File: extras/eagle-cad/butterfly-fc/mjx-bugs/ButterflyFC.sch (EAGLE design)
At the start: 5 parts

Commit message: Added sodler pads
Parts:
- added PAD1, PAD10, PAD2, PAD3, PAD4, PAD5, PAD6, PAD7, PAD8, PAD9: (no value), wirepad:SMD5
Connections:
- net GND: now also PAD10.P, PAD2.P, PAD4.P, PAD6.P, PAD8.P
- net VBAT: now also PAD1.P, PAD3.P, PAD5.P, PAD7.P, PAD9.P
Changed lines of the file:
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@@
 <part name="5VREG" library="SparkFun-Connectors" deviceset="CONN_03" device="1X03_NO_SILK"/>
 <part name="USFS" library="SparkFun-Connectors" deviceset="CONN_05" device="NO_SILK"/>
+<part name="PAD1" library="wirepad" deviceset="SMD5" device=""/>
+<part name="PAD2" library="wirepad" deviceset="SMD5" device=""/>
+<part name="PAD3" library="wirepad" deviceset="SMD5" device=""/>
+<part name="PAD4" library="wirepad" deviceset="SMD5" device=""/>
+<part name="PAD5" library="wirepad" deviceset="SMD5" device=""/>
+<part name="PAD6" library="wirepad" deviceset="SMD5" device=""/>
+<part name="PAD7" library="wirepad" deviceset="SMD5" device=""/>
+<part name="PAD8" library="wirepad" deviceset="SMD5" device=""/>
+<part name="PAD9" library="wirepad" deviceset="SMD5" device=""/>
+<part name="PAD10" library="wirepad" deviceset="SMD5" device=""/>
 </parts>
 <sheets>
@@
 <attribute name="NAME" x="38.1" y="56.388" size="1.778" layer="95" font="vector"/>
 </instance>
+<instance part="PAD1" gate="1" x="15.24" y="139.7" smashed="yes">
+<attribute name="VALUE" x="14.097" y="136.398" size="1.778" layer="96"/>
+</instance>
+<instance part="PAD2" gate="1" x="15.24" y="129.54" smashed="yes">
+<attribute name="VALUE" x="14.097" y="126.238" size="1.778" layer="96"/>
+</instance>
+<instance part="PAD3" gate="1" x="35.56" y="139.7" smashed="yes">
+<attribute name="VALUE" x="34.417" y="136.398" size="1.778" layer="96"/>
+</instance>
+<instance part="PAD4" gate="1" x="35.56" y="129.54" smashed="yes">
+<attribute name="VALUE" x="34.417" y="126.238" size="1.778" layer="96"/>
+</instance>
+<instance part="PAD5" gate="1" x="53.34" y="139.7" smashed="yes">
+<attribute name="VALUE" x="52.197" y="136.398" size="1.778" layer="96"/>
+</instance>
+<instance part="PAD6" gate="1" x="53.34" y="129.54" smashed="yes">
+<attribute name="VALUE" x="52.197" y="126.238" size="1.778" layer="96"/>
+</instance>
+<instance part="PAD7" gate="1" x="73.66" y="139.7" smashed="yes">
+<attribute name="VALUE" x="72.517" y="136.398" size="1.778" layer="96"/>
+</instance>
+<instance part="PAD8" gate="1" x="73.66" y="129.54" smashed="yes">
+<attribute name="VALUE" x="72.517" y="126.238" size="1.778" layer="96"/>
+</instance>
+<instance part="PAD9" gate="1" x="91.44" y="139.7" smashed="yes">
+<attribute name="VALUE" x="90.297" y="136.398" size="1.778" layer="96"/>
+</instance>
+<instance part="PAD10" gate="1" x="91.44" y="129.54" smashed="yes">
+<attribute name="VALUE" x="90.297" y="126.238" size="1.778" layer="96"/>
+</instance>
 </instances>
 <busses>
@@
 <label x="48.26" y="53.34" size="1.778" layer="95"/>
 </segment>
+<segment>
+<pinref part="PAD2" gate="1" pin="P"/>
+<wire x1="17.78" y1="129.54" x2="22.86" y2="129.54" width="0.1524" layer="91"/>
+<label x="17.78" y="129.54" size="1.778" layer="95"/>
+</segment>
+<segment>
+<pinref part="PAD4" gate="1" pin="P"/>
+<wire x1="38.1" y1="129.54" x2="43.18" y2="129.54" width="0.1524" layer="91"/>
+<label x="38.1" y="129.54" size="1.778" layer="95"/>
+</segment>
+<segment>
+<pinref part="PAD6" gate="1" pin="P"/>
+<wire x1="55.88" y1="129.54" x2="60.96" y2="129.54" width="0.1524" layer="91"/>
+<label x="55.88" y="129.54" size="1.778" layer="95"/>
+</segment>
+<segment>
+<pinref part="PAD8" gate="1" pin="P"/>
+<wire x1="76.2" y1="129.54" x2="81.28" y2="129.54" width="0.1524" layer="91"/>
+<label x="76.2" y="129.54" size="1.778" layer="95"/>
+</segment>
+<segment>
+<pinref part="PAD10" gate="1" pin="P"/>
+<wire x1="93.98" y1="129.54" x2="99.06" y2="129.54" width="0.1524" layer="91"/>
+<label x="93.98" y="129.54" size="1.778" layer="95"/>
+</segment>
 </net>
 <net name="5V" class="0">
@@
 <label x="53.34" y="78.74" size="1.778" layer="95"/>
 </segment>
-</net>
+<segment>
+<pinref part="PAD1" gate="1" pin="P"/>
+<wire x1="17.78" y1="139.7" x2="22.86" y2="139.7" width="0.1524" layer="91"/>
+<label x="17.78" y="139.7" size="1.778" layer="95"/>
+</segment>
+<segment>
+<pinref part="PAD3" gate="1" pin="P"/>
+<wire x1="38.1" y1="139.7" x2="43.18" y2="139.7" width="0.1524" layer="91"/>
+<label x="38.1" y="139.7" size="1.778" layer="95"/>
+</segment>
+<segment>
+<pinref part="PAD5" gate="1" pin="P"/>
+<wire x1="55.88" y1="139.7" x2="60.96" y2="139.7" width="0.1524" layer="91"/>
+<label x="55.88" y="139.7" size="1.778" layer="95"/>
+</segment>
+<segment>
+<pinref part="PAD7" gate="1" pin="P"/>
+<wire x1="76.2" y1="139.7" x2="81.28" y2="139.7" width="0.1524" layer="91"/>
+<label x="76.2" y="139.7" size="1.778" layer="95"/>
+</segment>
+<segment>
+<pinref part="PAD9" gate="1" pin="P"/>
+<wire x1="93.98" y1="139.7" x2="99.06" y2="139.7" width="0.1524" layer="91"/>
+<label x="93.98" y="139.7" size="1.778" layer="95"/>
+</segment>
+</net>

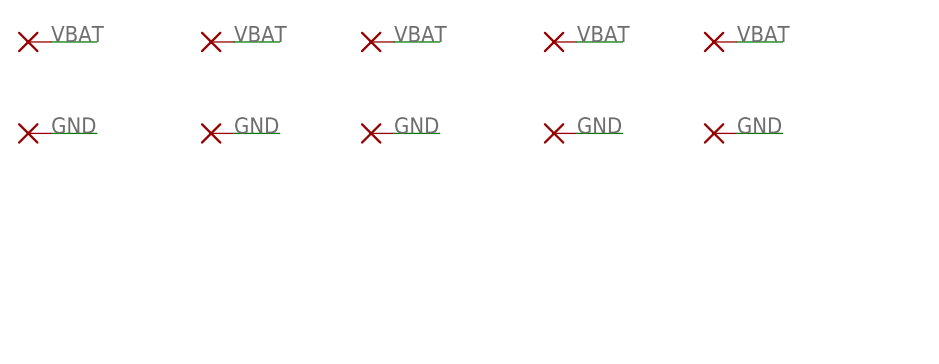
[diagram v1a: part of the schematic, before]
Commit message: Adjusted holes in board
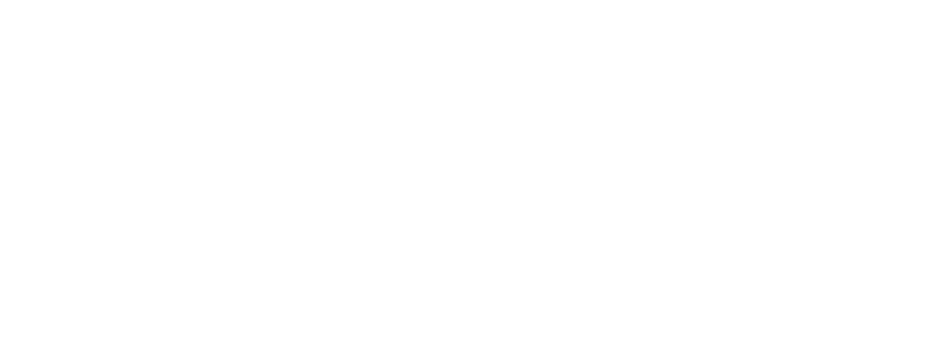
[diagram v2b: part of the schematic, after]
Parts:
- removed PAD1, PAD10, PAD2, PAD3, PAD4, PAD5, PAD6, PAD7, PAD8, PAD9: (no value), wirepad:SMD5
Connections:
- net GND: no longer PAD10.P, PAD2.P, PAD4.P, PAD6.P, PAD8.P
- net VBAT: no longer PAD1.P, PAD3.P, PAD5.P, PAD7.P, PAD9.P
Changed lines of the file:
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@@
 <part name="5VREG" library="SparkFun-Connectors" deviceset="CONN_03" device="1X03_NO_SILK"/>
 <part name="USFS" library="SparkFun-Connectors" deviceset="CONN_05" device="NO_SILK"/>
-<part name="PAD1" library="wirepad" deviceset="SMD5" device=""/>
-<part name="PAD2" library="wirepad" deviceset="SMD5" device=""/>
-<part name="PAD3" library="wirepad" deviceset="SMD5" device=""/>
-<part name="PAD4" library="wirepad" deviceset="SMD5" device=""/>
-<part name="PAD5" library="wirepad" deviceset="SMD5" device=""/>
-<part name="PAD6" library="wirepad" deviceset="SMD5" device=""/>
-<part name="PAD7" library="wirepad" deviceset="SMD5" device=""/>
-<part name="PAD8" library="wirepad" deviceset="SMD5" device=""/>
-<part name="PAD9" library="wirepad" deviceset="SMD5" device=""/>
-<part name="PAD10" library="wirepad" deviceset="SMD5" device=""/>
 </parts>
 <sheets>
@@
 <attribute name="VALUE" x="38.1" y="38.354" size="1.778" layer="96" font="vector"/>
 <attribute name="NAME" x="38.1" y="56.388" size="1.778" layer="95" font="vector"/>
-</instance>
-<instance part="PAD1" gate="1" x="15.24" y="139.7" smashed="yes">
-<attribute name="VALUE" x="14.097" y="136.398" size="1.778" layer="96"/>
-</instance>
-<instance part="PAD2" gate="1" x="15.24" y="129.54" smashed="yes">
-<attribute name="VALUE" x="14.097" y="126.238" size="1.778" layer="96"/>
-</instance>
-<instance part="PAD3" gate="1" x="35.56" y="139.7" smashed="yes">
-<attribute name="VALUE" x="34.417" y="136.398" size="1.778" layer="96"/>
-</instance>
-<instance part="PAD4" gate="1" x="35.56" y="129.54" smashed="yes">
-<attribute name="VALUE" x="34.417" y="126.238" size="1.778" layer="96"/>
-</instance>
-<instance part="PAD5" gate="1" x="53.34" y="139.7" smashed="yes">
-<attribute name="VALUE" x="52.197" y="136.398" size="1.778" layer="96"/>
-</instance>
-<instance part="PAD6" gate="1" x="53.34" y="129.54" smashed="yes">
-<attribute name="VALUE" x="52.197" y="126.238" size="1.778" layer="96"/>
-</instance>
-<instance part="PAD7" gate="1" x="73.66" y="139.7" smashed="yes">
-<attribute name="VALUE" x="72.517" y="136.398" size="1.778" layer="96"/>
-</instance>
-<instance part="PAD8" gate="1" x="73.66" y="129.54" smashed="yes">
-<attribute name="VALUE" x="72.517" y="126.238" size="1.778" layer="96"/>
-</instance>
-<instance part="PAD9" gate="1" x="91.44" y="139.7" smashed="yes">
-<attribute name="VALUE" x="90.297" y="136.398" size="1.778" layer="96"/>
-</instance>
-<instance part="PAD10" gate="1" x="91.44" y="129.54" smashed="yes">
-<attribute name="VALUE" x="90.297" y="126.238" size="1.778" layer="96"/>
 </instance>
 </instances>
@@
 <wire x1="48.26" y1="53.34" x2="53.34" y2="53.34" width="0.1524" layer="91"/>
 <label x="48.26" y="53.34" size="1.778" layer="95"/>
-</segment>
-<segment>
-<pinref part="PAD2" gate="1" pin="P"/>
-<wire x1="17.78" y1="129.54" x2="22.86" y2="129.54" width="0.1524" layer="91"/>
-<label x="17.78" y="129.54" size="1.778" layer="95"/>
-</segment>
-<segment>
-<pinref part="PAD4" gate="1" pin="P"/>
-<wire x1="38.1" y1="129.54" x2="43.18" y2="129.54" width="0.1524" layer="91"/>
-<label x="38.1" y="129.54" size="1.778" layer="95"/>
-</segment>
-<segment>
-<pinref part="PAD6" gate="1" pin="P"/>
-<wire x1="55.88" y1="129.54" x2="60.96" y2="129.54" width="0.1524" layer="91"/>
-<label x="55.88" y="129.54" size="1.778" layer="95"/>
-</segment>
-<segment>
-<pinref part="PAD8" gate="1" pin="P"/>
-<wire x1="76.2" y1="129.54" x2="81.28" y2="129.54" width="0.1524" layer="91"/>
-<label x="76.2" y="129.54" size="1.778" layer="95"/>
-</segment>
-<segment>
-<pinref part="PAD10" gate="1" pin="P"/>
-<wire x1="93.98" y1="129.54" x2="99.06" y2="129.54" width="0.1524" layer="91"/>
-<label x="93.98" y="129.54" size="1.778" layer="95"/>
 </segment>
 </net>
@@
 <label x="53.34" y="78.74" size="1.778" layer="95"/>
 </segment>
-<segment>
-<pinref part="PAD1" gate="1" pin="P"/>
-<wire x1="17.78" y1="139.7" x2="22.86" y2="139.7" width="0.1524" layer="91"/>
-<label x="17.78" y="139.7" size="1.778" layer="95"/>
-</segment>
-<segment>
-<pinref part="PAD3" gate="1" pin="P"/>
-<wire x1="38.1" y1="139.7" x2="43.18" y2="139.7" width="0.1524" layer="91"/>
-<label x="38.1" y="139.7" size="1.778" layer="95"/>
-</segment>
-<segment>
-<pinref part="PAD5" gate="1" pin="P"/>
-<wire x1="55.88" y1="139.7" x2="60.96" y2="139.7" width="0.1524" layer="91"/>
-<label x="55.88" y="139.7" size="1.778" layer="95"/>
-</segment>
-<segment>
-<pinref part="PAD7" gate="1" pin="P"/>
-<wire x1="76.2" y1="139.7" x2="81.28" y2="139.7" width="0.1524" layer="91"/>
-<label x="76.2" y="139.7" size="1.778" layer="95"/>
-</segment>
-<segment>
-<pinref part="PAD9" gate="1" pin="P"/>
-<wire x1="93.98" y1="139.7" x2="99.06" y2="139.7" width="0.1524" layer="91"/>
-<label x="93.98" y="139.7" size="1.778" layer="95"/>
-</segment>
 </net>

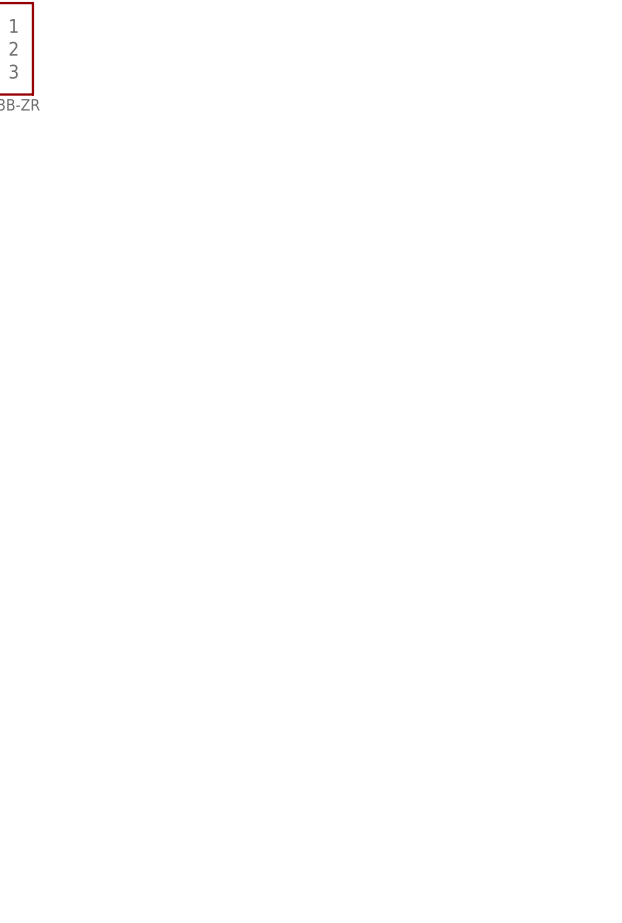
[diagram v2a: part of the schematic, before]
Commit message: Added solder pads
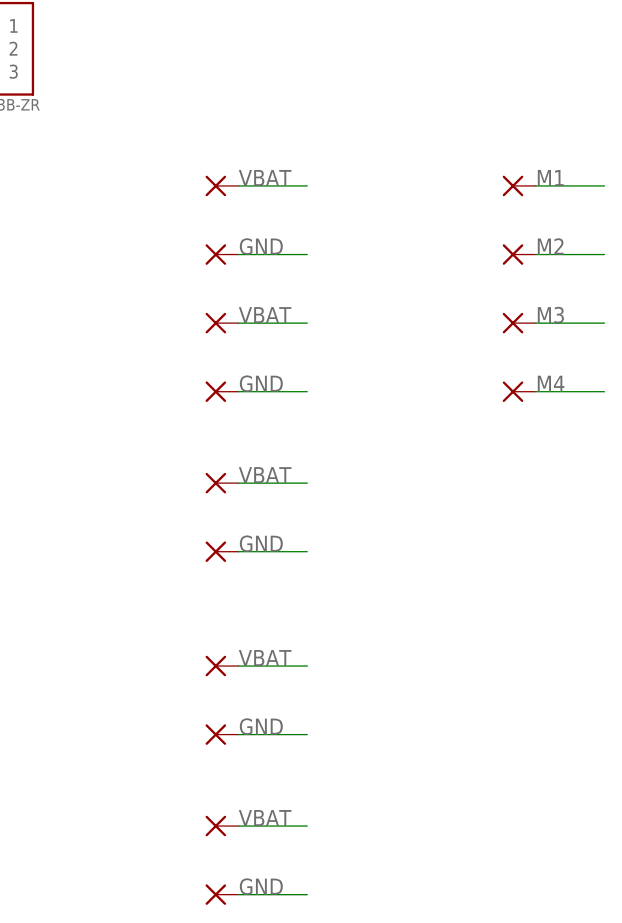
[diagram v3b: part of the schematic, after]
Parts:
- added PAD1, PAD10, PAD11, PAD12, PAD13, PAD14, PAD2, PAD3, PAD4, PAD5, PAD6, PAD7, PAD8, PAD9: WIREPADSMD5-2,5, wirepad:WIREPADSMD5-2,5
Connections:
- new net M4: PAD12.P
- net GND: now also PAD10.P, PAD2.P, PAD4.P, PAD6.P, PAD8.P
- net M1: now also PAD13.P
- net M2: now also PAD14.P
- net M3: now also PAD11.P
- net VBAT: now also PAD1.P, PAD3.P, PAD5.P, PAD7.P, PAD9.P
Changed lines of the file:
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@@
 <part name="5VREG" library="SparkFun-Connectors" deviceset="CONN_03" device="1X03_NO_SILK"/>
 <part name="USFS" library="SparkFun-Connectors" deviceset="CONN_05" device="NO_SILK"/>
+<part name="PAD1" library="wirepad" deviceset="WIREPAD" device="SMD5-2,5"/>
+<part name="PAD2" library="wirepad" deviceset="WIREPAD" device="SMD5-2,5"/>
+<part name="PAD3" library="wirepad" deviceset="WIREPAD" device="SMD5-2,5"/>
+<part name="PAD4" library="wirepad" deviceset="WIREPAD" device="SMD5-2,5"/>
+<part name="PAD5" library="wirepad" deviceset="WIREPAD" device="SMD5-2,5"/>
+<part name="PAD6" library="wirepad" deviceset="WIREPAD" device="SMD5-2,5"/>
+<part name="PAD7" library="wirepad" deviceset="WIREPAD" device="SMD5-2,5"/>
+<part name="PAD8" library="wirepad" deviceset="WIREPAD" device="SMD5-2,5"/>
+<part name="PAD9" library="wirepad" deviceset="WIREPAD" device="SMD5-2,5"/>
+<part name="PAD10" library="wirepad" deviceset="WIREPAD" device="SMD5-2,5"/>
+<part name="PAD11" library="wirepad" deviceset="WIREPAD" device="SMD5-2,5"/>
+<part name="PAD12" library="wirepad" deviceset="WIREPAD" device="SMD5-2,5"/>
+<part name="PAD13" library="wirepad" deviceset="WIREPAD" device="SMD5-2,5"/>
+<part name="PAD14" library="wirepad" deviceset="WIREPAD" device="SMD5-2,5"/>
 </parts>
 <sheets>
@@
 <attribute name="NAME" x="38.1" y="56.388" size="1.778" layer="95" font="vector"/>
 </instance>
+<instance part="PAD1" gate="G$1" x="132.08" y="63.5" smashed="yes"/>
+<instance part="PAD2" gate="G$1" x="132.08" y="55.88" smashed="yes"/>
+<instance part="PAD3" gate="G$1" x="132.08" y="45.72" smashed="yes"/>
+<instance part="PAD4" gate="G$1" x="132.08" y="38.1" smashed="yes"/>
+<instance part="PAD5" gate="G$1" x="132.08" y="25.4" smashed="yes"/>
+<instance part="PAD6" gate="G$1" x="132.08" y="17.78" smashed="yes"/>
+<instance part="PAD7" gate="G$1" x="132.08" y="7.62" smashed="yes"/>
+<instance part="PAD8" gate="G$1" x="132.08" y="0" smashed="yes"/>
+<instance part="PAD9" gate="G$1" x="132.08" y="78.74" smashed="yes"/>
+<instance part="PAD10" gate="G$1" x="132.08" y="71.12" smashed="yes"/>
+<instance part="PAD11" gate="G$1" x="165.1" y="63.5" smashed="yes"/>
+<instance part="PAD12" gate="G$1" x="165.1" y="55.88" smashed="yes"/>
+<instance part="PAD13" gate="G$1" x="165.1" y="78.74" smashed="yes"/>
+<instance part="PAD14" gate="G$1" x="165.1" y="71.12" smashed="yes"/>
 </instances>
 <busses>
@@
 <label x="48.26" y="53.34" size="1.778" layer="95"/>
 </segment>
+<segment>
+<pinref part="PAD2" gate="G$1" pin="P"/>
+<wire x1="134.62" y1="55.88" x2="142.24" y2="55.88" width="0.1524" layer="91"/>
+<label x="134.62" y="55.88" size="1.778" layer="95"/>
+</segment>
+<segment>
+<pinref part="PAD4" gate="G$1" pin="P"/>
+<wire x1="134.62" y1="38.1" x2="142.24" y2="38.1" width="0.1524" layer="91"/>
+<label x="134.62" y="38.1" size="1.778" layer="95"/>
+</segment>
+<segment>
+<pinref part="PAD6" gate="G$1" pin="P"/>
+<wire x1="134.62" y1="17.78" x2="142.24" y2="17.78" width="0.1524" layer="91"/>
+<label x="134.62" y="17.78" size="1.778" layer="95"/>
+</segment>
+<segment>
+<pinref part="PAD8" gate="G$1" pin="P"/>
+<wire x1="134.62" y1="0" x2="142.24" y2="0" width="0.1524" layer="91"/>
+<label x="134.62" y="0" size="1.778" layer="95"/>
+</segment>
+<segment>
+<pinref part="PAD10" gate="G$1" pin="P"/>
+<wire x1="134.62" y1="71.12" x2="142.24" y2="71.12" width="0.1524" layer="91"/>
+<label x="134.62" y="71.12" size="1.778" layer="95"/>
+</segment>
 </net>
 <net name="5V" class="0">
@@
 <label x="99.06" y="40.64" size="1.778" layer="95"/>
 </segment>
+<segment>
+<pinref part="PAD13" gate="G$1" pin="P"/>
+<wire x1="167.64" y1="78.74" x2="175.26" y2="78.74" width="0.1524" layer="91"/>
+<label x="167.64" y="78.74" size="1.778" layer="95"/>
+</segment>
 </net>
 <net name="M2" class="0">
@@
 <label x="99.06" y="43.18" size="1.778" layer="95"/>
 </segment>
+<segment>
+<pinref part="PAD14" gate="G$1" pin="P"/>
+<wire x1="167.64" y1="71.12" x2="175.26" y2="71.12" width="0.1524" layer="91"/>
+<label x="167.64" y="71.12" size="1.778" layer="95"/>
+</segment>
 </net>
 <net name="M3" class="0">
@@
 <label x="99.06" y="45.72" size="1.778" layer="95"/>
 </segment>
+<segment>
+<pinref part="PAD11" gate="G$1" pin="P"/>
+<wire x1="167.64" y1="63.5" x2="175.26" y2="63.5" width="0.1524" layer="91"/>
+<label x="167.64" y="63.5" size="1.778" layer="95"/>
+</segment>
 </net>
 <net name="SCL" class="0">
@@
 <label x="53.34" y="78.74" size="1.778" layer="95"/>
 </segment>
-</net>
+<segment>
+<pinref part="PAD1" gate="G$1" pin="P"/>
+<wire x1="134.62" y1="63.5" x2="142.24" y2="63.5" width="0.1524" layer="91"/>
+<label x="134.62" y="63.5" size="1.778" layer="95"/>
+</segment>
+<segment>
+<pinref part="PAD3" gate="G$1" pin="P"/>
+<wire x1="134.62" y1="45.72" x2="142.24" y2="45.72" width="0.1524" layer="91"/>
+<label x="134.62" y="45.72" size="1.778" layer="95"/>
+</segment>
+<segment>
+<pinref part="PAD5" gate="G$1" pin="P"/>
+<wire x1="134.62" y1="25.4" x2="142.24" y2="25.4" width="0.1524" layer="91"/>
+<label x="134.62" y="25.4" size="1.778" layer="95"/>
+</segment>
+<segment>
+<pinref part="PAD7" gate="G$1" pin="P"/>
+<wire x1="134.62" y1="7.62" x2="142.24" y2="7.62" width="0.1524" layer="91"/>
+<label x="134.62" y="7.62" size="1.778" layer="95"/>
+</segment>
+<segment>
+<pinref part="PAD9" gate="G$1" pin="P"/>
+<wire x1="134.62" y1="78.74" x2="142.24" y2="78.74" width="0.1524" layer="91"/>
+<label x="134.62" y="78.74" size="1.778" layer="95"/>
+</segment>
+</net>
+<net name="M4" class="0">
+<segment>
+<pinref part="PAD12" gate="G$1" pin="P"/>
+<wire x1="167.64" y1="55.88" x2="175.26" y2="55.88" width="0.1524" layer="91"/>
+<label x="167.64" y="55.88" size="1.778" layer="95"/>
+</segment>
+</net>

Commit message: More ButterflyFC work
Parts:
- added BLUE: (no value), SparkFun-Connectors:CONN_041X04_NO_SILK
- renumbered J1 to MCU1, J2 to MCU2
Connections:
- net RX renamed DSMX
- new net BLRX: BLUE.1
- new net BLTX: BLUE.2
- net 3V3: now also BLUE.4
- net GND: now also BLUE.3
